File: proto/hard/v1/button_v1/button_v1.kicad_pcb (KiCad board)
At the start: 2 copper layers, 108.9 x 76.9 mm, 140 parts, among them J1 Conn_01x06_Female, J10 Conn_01x01_Female, J11 Conn_01x01_Female, J12 Conn_01x01_Female, J13 Conn_01x01_Female, J14 K3-2336D-combi, J15 Conn_01x03_Male, J16 Conn_01x01_Male, J2 Conn_01x06_Female, J3 Conn_01x06_Female, J4 Conn_01x06_Female, J5 USB_B_Micro, J6 Conn_01x08_Female, J7 Conn_01x04_Female, J8 AudioJack3, J9 Conn_01x01_Female, Q1 TP0610T, Q2 IRLML2060, Q3 TP0610T, Q4 IRLML2060, Q5 IRLML2060, Q6 UMG8N, Q7 UMG8N, Q8 TP0610T, U1 LCD_2.8_SPI, U10 NL27WZ14, U11 TC305, U12 OLED_0.96_I2C, U13 74HC595, U2 STM32F103C8Tx, U3 RT8009-33, U4 RClamp0554S, U5 RT9293, U6 LM339, U7 AP1117-33, U8 ST485EBDR, U9 LM358, Y1 8MHz

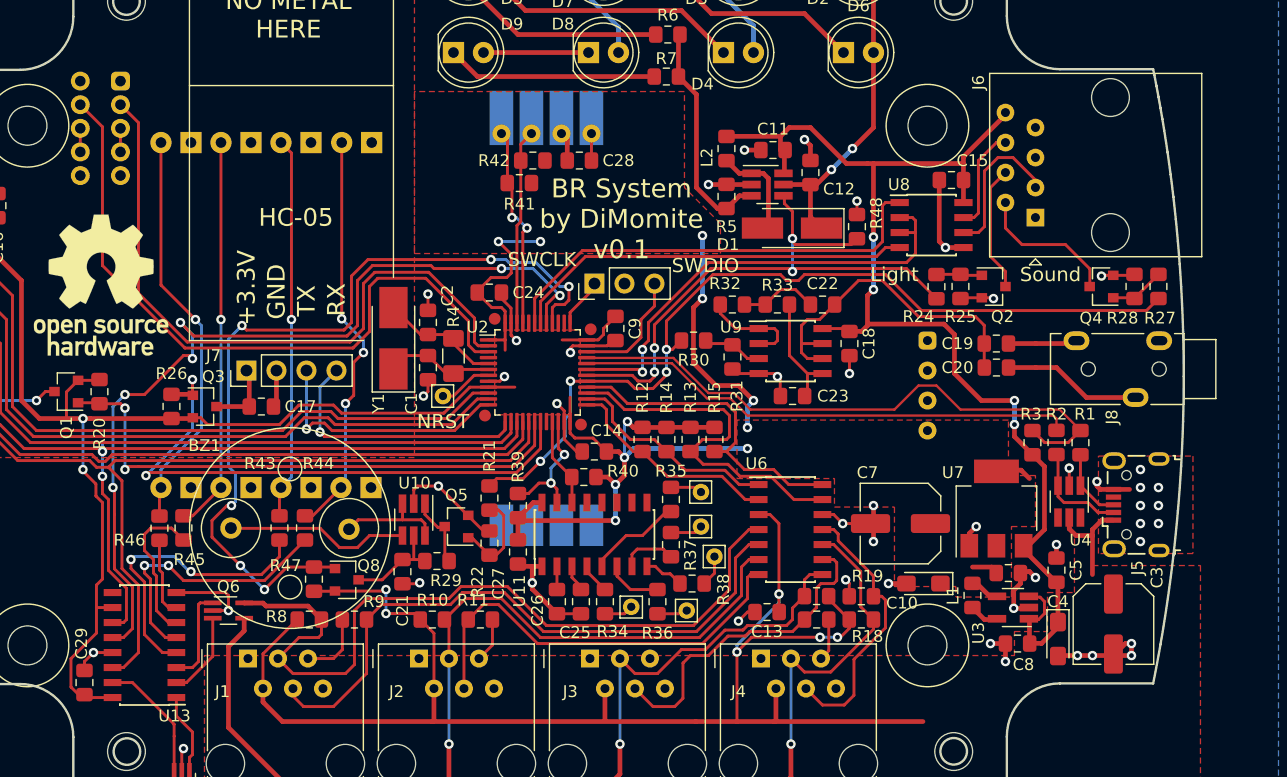
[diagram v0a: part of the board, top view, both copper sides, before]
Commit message: Schematic libs clean-up
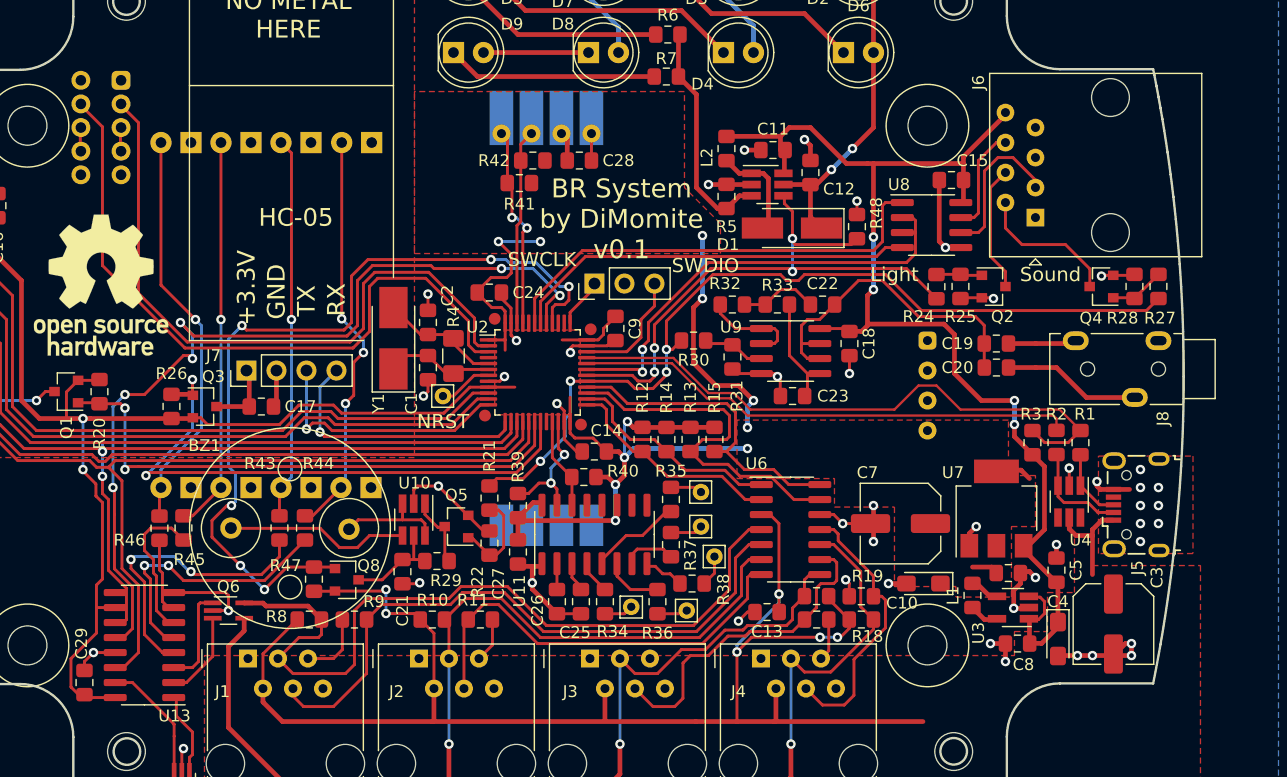
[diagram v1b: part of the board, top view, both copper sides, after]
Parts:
- J14: footprint MyConnectors:K3-2346D -> brbuttonsystem:K3-2346D
- J8: footprint MyConnectors:PJ-001-H -> brbuttonsystem:PJ-001-H
- moved J14 0.08 mm to (85.7, 71.1)
- moved J8 0.06 mm to (177.4, 91.6)
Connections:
- U12 pad 5: GND -> Net-(U12-Pad5)

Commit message: Added example project with button connection schematic only. Corrected "dip" pins assignment to comply with main project.
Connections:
- R12 pad 1: /But1 -> /But0
- R14 pad 1: /But0 -> /But1
- U2 pad 25: /But1 -> /But0
- U2 pad 26: /But0 -> /But1
- U6 pad 1: /But0 -> /But1
- U6 pad 2: /But1 -> /But0
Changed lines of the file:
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@@
       (net 20 +3V3))
     (pad 1 smd roundrect (at -1.025 0 90) (size 1.15 1.4) (layers F.Cu F.Paste F.Mask) (roundrect_rratio 0.217391)
-      (net 39 /But0))
+      (net 38 /But1))
     (model ${KISYS3DMOD}/Resistor_SMD.3dshapes/R_0805_2012Metric.wrl
       (at (xyz 0 0 0))
@@
       (net 20 +3V3))
     (pad 1 smd roundrect (at -1.025 0 90) (size 1.15 1.4) (layers F.Cu F.Paste F.Mask) (roundrect_rratio 0.217391)
-      (net 38 /But1))
+      (net 39 /But0))
     (model ${KISYS3DMOD}/Resistor_SMD.3dshapes/R_0805_2012Metric.wrl
       (at (xyz 0 0 0))
@@
       (net 19 +5V))
     (pad 2 smd roundrect (at -2.475 -2.54) (size 1.95 0.6) (layers F.Cu F.Paste F.Mask) (roundrect_rratio 0.25)
+      (net 39 /But0))
+    (pad 1 smd roundrect (at -2.475 -3.81) (size 1.95 0.6) (layers F.Cu F.Paste F.Mask) (roundrect_rratio 0.25)
       (net 38 /But1))
-    (pad 1 smd roundrect (at -2.475 -3.81) (size 1.95 0.6) (layers F.Cu F.Paste F.Mask) (roundrect_rratio 0.25)
-      (net 39 /But0))
     (model ${KISYS3DMOD}/Package_SO.3dshapes/SOIC-14_3.9x8.7mm_P1.27mm.wrl
       (at (xyz 0 0 0))
@@
       (net 37 /But2))
     (pad 26 smd roundrect (at 4.1625 2.25) (size 1.475 0.3) (layers F.Cu F.Paste F.Mask) (roundrect_rratio 0.25)
+      (net 38 /But1))
+    (pad 25 smd roundrect (at 4.1625 2.75) (size 1.475 0.3) (layers F.Cu F.Paste F.Mask) (roundrect_rratio 0.25)
       (net 39 /But0))
-    (pad 25 smd roundrect (at 4.1625 2.75) (size 1.475 0.3) (layers F.Cu F.Paste F.Mask) (roundrect_rratio 0.25)
-      (net 38 /But1))
     (pad 24 smd roundrect (at 2.75 4.1625) (size 0.3 1.475) (layers F.Cu F.Paste F.Mask) (roundrect_rratio 0.25)
       (net 20 +3V3))
@@
   (segment (start 138.938 95.504) (end 138.938 97.282) (width 0.25) (layer F.Cu) (net 37))
   (segment (start 138.938 97.282) (end 138.684 97.536) (width 0.25) (layer F.Cu) (net 37))
-  (segment (start 130.81 98.552) (end 131.572 98.552) (width 0.25) (layer F.Cu) (net 38))
-  (segment (start 128.524 96.266) (end 130.81 98.552) (width 0.25) (layer F.Cu) (net 38))
-  (segment (start 128.524 94.996) (end 128.524 96.266) (width 0.25) (layer F.Cu) (net 38))
-  (segment (start 126.8565 94.5995) (end 128.1275 94.5995) (width 0.25) (layer F.Cu) (net 38))
-  (segment (start 128.1275 94.5995) (end 128.524 94.996) (width 0.25) (layer F.Cu) (net 38))
-  (segment (start 140.2715 102.616) (end 141.412 102.616) (width 0.25) (layer F.Cu) (net 38))
-  (segment (start 138.306758 100.651258) (end 140.2715 102.616) (width 0.25) (layer F.Cu) (net 38))
-  (segment (start 131.572 98.552) (end 133.671258 100.651258) (width 0.25) (layer F.Cu) (net 38))
-  (segment (start 133.671258 100.651258) (end 138.306758 100.651258) (width 0.25) (layer F.Cu) (net 38))
-  (segment (start 128.3895 94.0995) (end 126.8565 94.0995) (width 0.25) (layer F.Cu) (net 39))
-  (segment (start 133.604 98.552) (end 132.588 97.536) (width 0.25) (layer F.Cu) (net 39))
-  (segment (start 133.604 98.561) (end 133.604 98.552) (width 0.25) (layer F.Cu) (net 39))
-  (segment (start 132.588 97.536) (end 130.556 97.536) (width 0.25) (layer F.Cu) (net 39))
-  (segment (start 130.556 97.536) (end 129.032 96.012) (width 0.25) (layer F.Cu) (net 39))
-  (segment (start 129.032 96.012) (end 129.032 94.742) (width 0.25) (layer F.Cu) (net 39))
-  (segment (start 129.032 94.742) (end 128.3895 94.0995) (width 0.25) (layer F.Cu) (net 39))
-  (segment (start 139.7635 101.346) (end 141.412 101.346) (width 0.25) (layer F.Cu) (net 39))
-  (segment (start 138.557 100.1395) (end 139.7635 101.346) (width 0.25) (layer F.Cu) (net 39))
-  (segment (start 135.1915 100.1395) (end 138.557 100.1395) (width 0.25) (layer F.Cu) (net 39))
-  (segment (start 133.604 98.561) (end 133.613 98.561) (width 0.25) (layer F.Cu) (net 39))
-  (segment (start 133.613 98.561) (end 135.1915 100.1395) (width 0.25) (layer F.Cu) (net 39))
+  (segment (start 130.81 98.552) (end 131.572 98.552) (width 0.25) (layer F.Cu) (net 39))
+  (segment (start 128.524 96.266) (end 130.81 98.552) (width 0.25) (layer F.Cu) (net 39))
+  (segment (start 128.524 94.996) (end 128.524 96.266) (width 0.25) (layer F.Cu) (net 39))
+  (segment (start 126.8565 94.5995) (end 128.1275 94.5995) (width 0.25) (layer F.Cu) (net 39))
+  (segment (start 128.1275 94.5995) (end 128.524 94.996) (width 0.25) (layer F.Cu) (net 39))
+  (segment (start 140.2715 102.616) (end 141.412 102.616) (width 0.25) (layer F.Cu) (net 39))
+  (segment (start 138.306758 100.651258) (end 140.2715 102.616) (width 0.25) (layer F.Cu) (net 39))
+  (segment (start 131.572 98.552) (end 133.671258 100.651258) (width 0.25) (layer F.Cu) (net 39))
+  (segment (start 133.671258 100.651258) (end 138.306758 100.651258) (width 0.25) (layer F.Cu) (net 39))
+  (segment (start 128.3895 94.0995) (end 126.8565 94.0995) (width 0.25) (layer F.Cu) (net 38))
+  (segment (start 133.604 98.552) (end 132.588 97.536) (width 0.25) (layer F.Cu) (net 38))
+  (segment (start 133.604 98.561) (end 133.604 98.552) (width 0.25) (layer F.Cu) (net 38))
+  (segment (start 132.588 97.536) (end 130.556 97.536) (width 0.25) (layer F.Cu) (net 38))
+  (segment (start 130.556 97.536) (end 129.032 96.012) (width 0.25) (layer F.Cu) (net 38))
+  (segment (start 129.032 96.012) (end 129.032 94.742) (width 0.25) (layer F.Cu) (net 38))
+  (segment (start 129.032 94.742) (end 128.3895 94.0995) (width 0.25) (layer F.Cu) (net 38))
+  (segment (start 139.7635 101.346) (end 141.412 101.346) (width 0.25) (layer F.Cu) (net 38))
+  (segment (start 138.557 100.1395) (end 139.7635 101.346) (width 0.25) (layer F.Cu) (net 38))
+  (segment (start 135.1915 100.1395) (end 138.557 100.1395) (width 0.25) (layer F.Cu) (net 38))
+  (segment (start 133.604 98.561) (end 133.613 98.561) (width 0.25) (layer F.Cu) (net 38))
+  (segment (start 133.613 98.561) (end 135.1915 100.1395) (width 0.25) (layer F.Cu) (net 38))
   (segment (start 76.835 96.774) (end 74.422 96.774) (width 0.25) (layer F.Cu) (net 49))
   (segment (start 78.867 98.806) (end 76.835 96.774) (width 0.25) (layer F.Cu) (net 49))

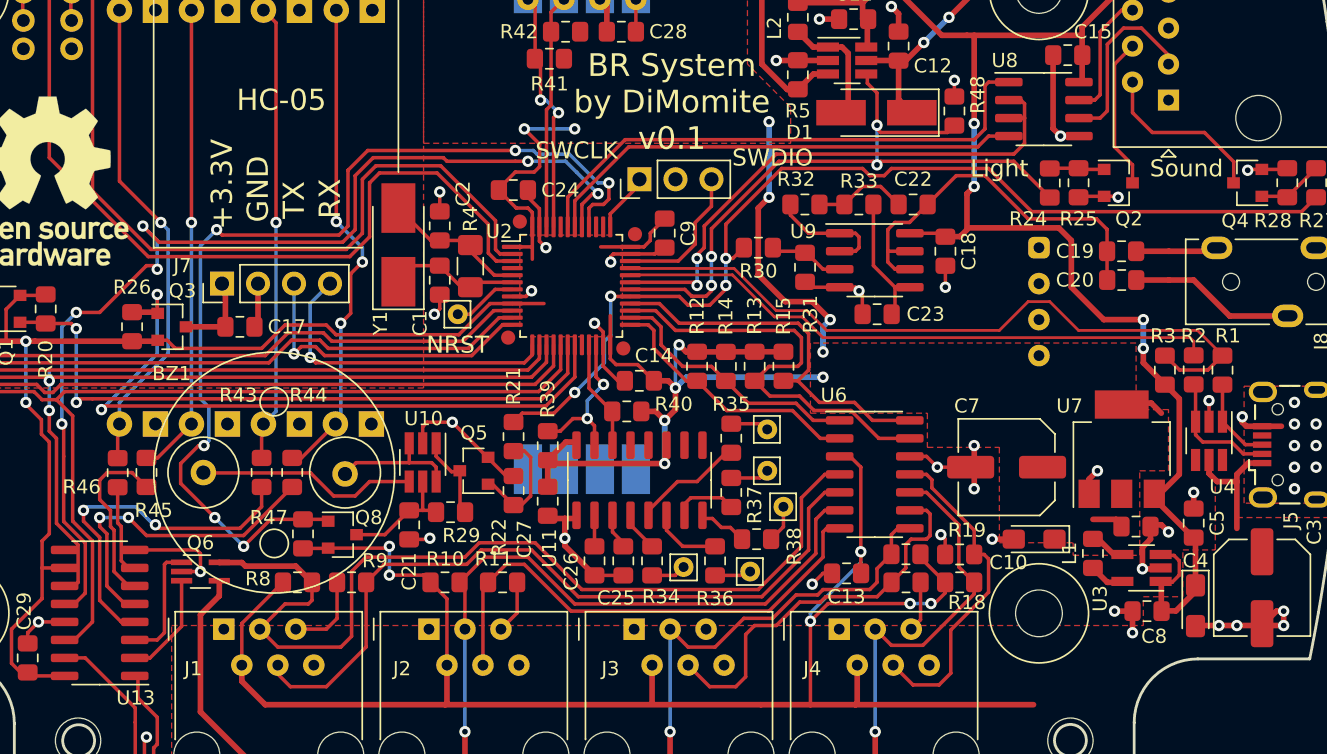
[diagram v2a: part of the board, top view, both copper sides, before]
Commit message: Fixed RClamp0554S wrong pinout. Corrected schematic and PCB. Added text for ICs on board.
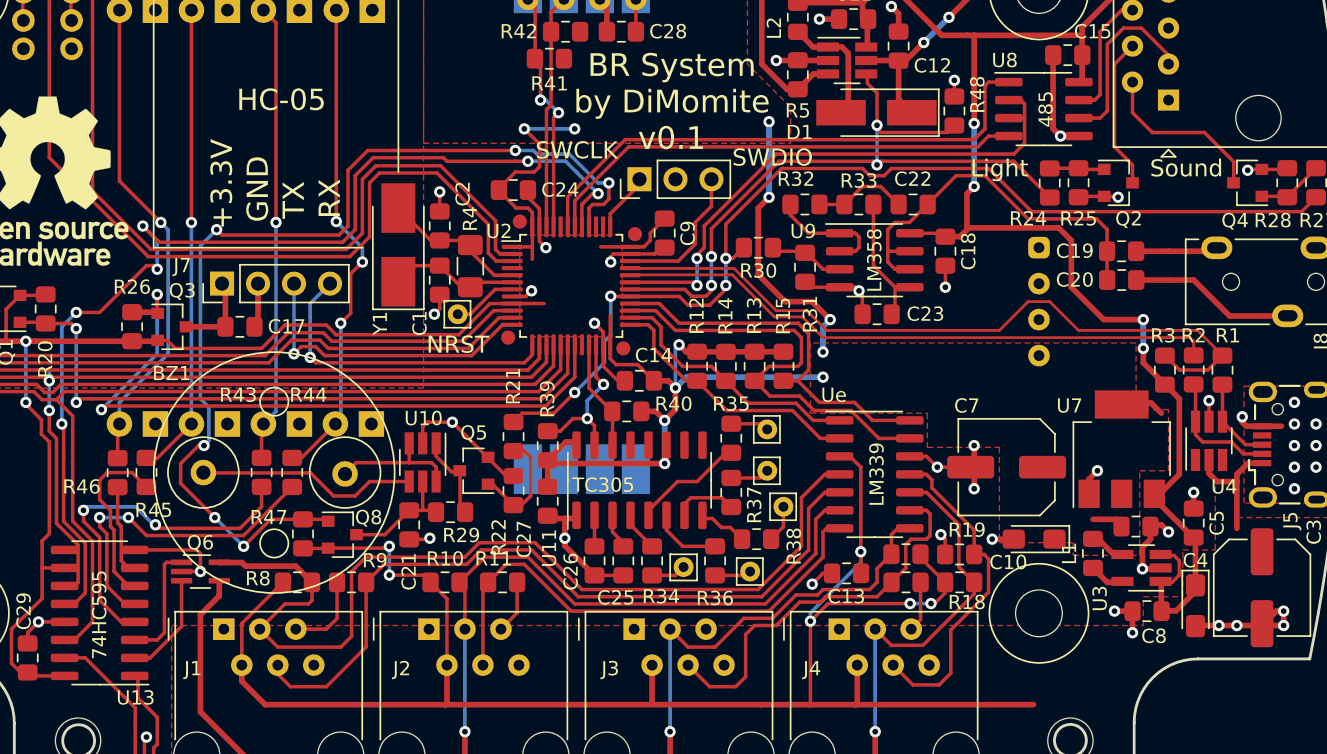
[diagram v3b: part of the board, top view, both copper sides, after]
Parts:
- removed U6: LM339, Package_SO:SOIC-14_3.9x8.7mm_P1.27mm
- added Ue: LM339, Package_SO:SOIC-14_3.9x8.7mm_P1.27mm, F.Cu at (144.1, 105.2)
- R3: value 4k7 -> 1k5
- U8: value ST485EBDR -> 485
- turned U4 to 90 degrees
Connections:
- U4 pad 1: /PowerInput/USB_P -> Net-(U4-Pad1)
- U4 pad 2: GND -> +5V
- U4 pad 3: /PowerInput/USB_N -> Net-(U4-Pad3)
- U4 pad 4: Net-(U4-Pad4) -> /PowerInput/USB_P
- U4 pad 5: +5V -> GND
- U4 pad 6: Net-(U4-Pad6) -> /PowerInput/USB_N
